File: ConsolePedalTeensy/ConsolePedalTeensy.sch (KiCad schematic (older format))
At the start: 27 parts, among them J1 Conn_02x25_Counter_Clockwise, SW1 SW_Push, SW2 SW_Push, U1 Teensy3.2, U2 LM7805_TO220

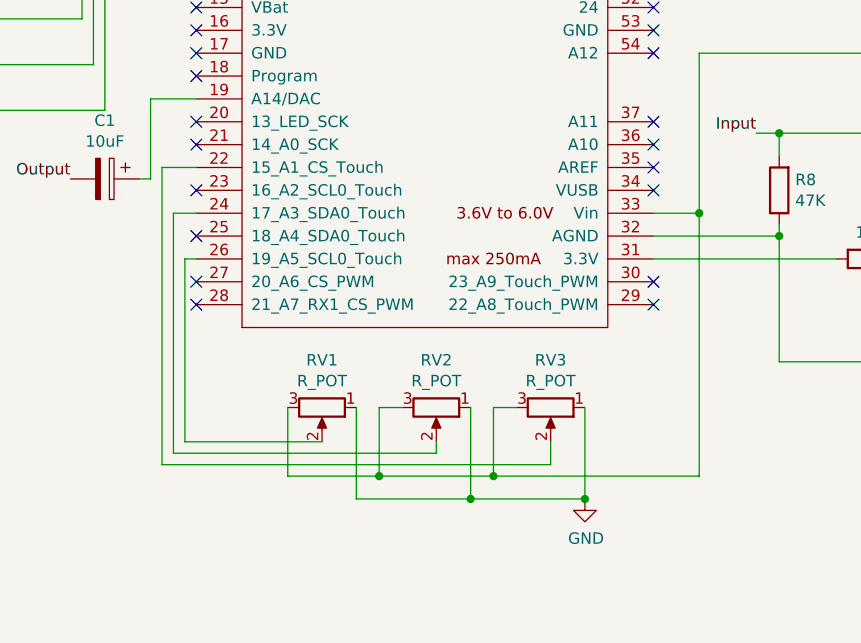
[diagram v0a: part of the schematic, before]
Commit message: Finished placement of components
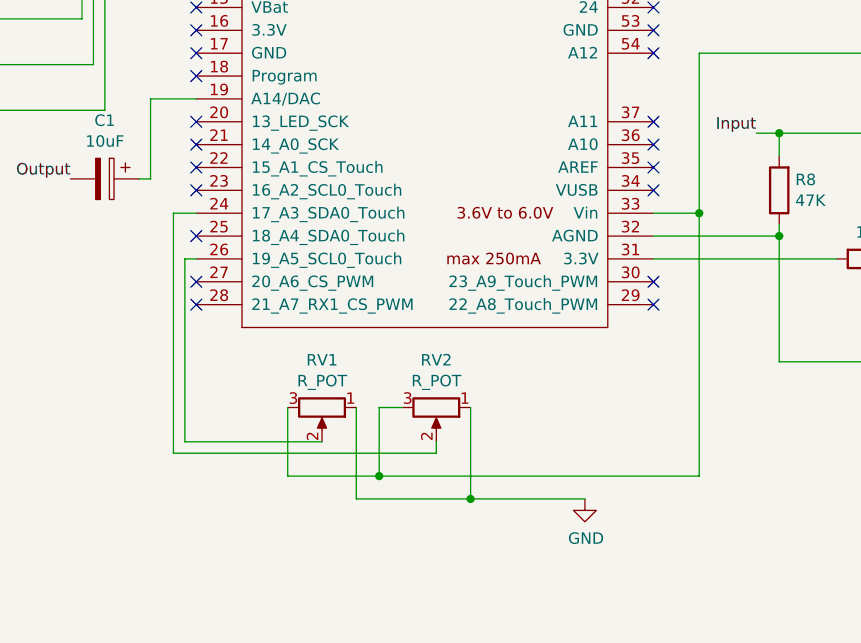
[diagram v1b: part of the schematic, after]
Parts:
- removed RV3: R_POT, Potentiometer_THT:Potentiometer_Bourns_PTV09A-1_Single_Vertical, symbol Device:R_POT
- U1: footprint teensy:Teensy30_31_32_All_Pins -> libraries:Teensy3.2
- U2: footprint Package_TO_SOT_THT:TO-220-3_Vertical -> Package_TO_SOT_THT:TO-220-3_Horizontal_TabDown
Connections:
- no-connect marks 64 -> 65
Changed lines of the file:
@@
 F 0 "U1" H 5200 4237 60  0000 C CNN
 F 1 "Teensy3.2" H 5200 4131 60  0000 C CNN
-F 2 "teensy:Teensy30_31_32_All_Pins" H 5200 1850 60  0001 C CNN
+F 2 "libraries:Teensy3.2" H 5200 1850 60  0001 C CNN
 F 3 "" H 5200 1850 60  0000 C CNN
 	1    5200 2600
@@
 F 0 "U2" H 7300 2142 50  0000 C CNN
 F 1 "LM7805_TO220" H 7300 2051 50  0000 C CNN
-F 2 "Package_TO_SOT_THT:TO-220-3_Vertical" H 7300 2125 50  0001 C CIN
+F 2 "Package_TO_SOT_THT:TO-220-3_Horizontal_TabDown" H 7300 2125 50  0001 C CIN
 F 3 "https://www.onsemi.cn/PowerSolutions/document/MC7800-D.PDF" H 7300 1850 50  0001 C CNN
 	1    7300 1900
@@
 	0    1    1    0
 $EndComp
-$Comp
-L Device:R_POT RV3
-U 1 1 602F1C1B
-P 5750 4400
-F 0 "RV3" V 5543 4400 50  0000 C CNN
-F 1 "R_POT" V 5634 4400 50  0000 C CNN
-F 2 "Potentiometer_THT:Potentiometer_Bourns_PTV09A-1_Single_Vertical" H 5750 4400 50  0001 C CNN
-F 3 "~" H 5750 4400 50  0001 C CNN
-	1    5750 4400
-	0    1    1    0
-$EndComp
 Wire Wire Line
 	4600 4400 4600 4700
@@
 Wire Wire Line
 	5000 4400 5100 4400
-Wire Wire Line
-	5600 4400 5500 4400
-Wire Wire Line
-	5500 4400 5500 4700
-Wire Wire Line
-	5500 4700 5000 4700
 Connection ~ 5000 4700
 Wire Wire Line
@@
 Wire Wire Line
 	5400 4800 5900 4800
-Wire Wire Line
-	5900 4800 5900 4400
 Connection ~ 5400 4800
 $Comp
@@
 	1    0    0    -1
 $EndComp
-Connection ~ 5900 4800
-Wire Wire Line
-	5500 4700 6400 4700
 Wire Wire Line
 	6400 4700 6400 3550
-Connection ~ 5500 4700
 Connection ~ 6400 3550
 Wire Wire Line
@@
 	5250 4600 4100 4600
 Wire Wire Line
-	5750 4550 5750 4650
-Wire Wire Line
-	5750 4650 4050 4650
-Wire Wire Line
 	4150 3750 4200 3750
 Wire Wire Line
@@
 Wire Wire Line
 	4100 3550 4100 4600
-Wire Wire Line
-	4050 3350 4200 3350
-Wire Wire Line
-	4050 3350 4050 4650
 $Comp
 L Device:LED_RGBC D3
@@
 NoConn ~ 6200 1350
 NoConn ~ 6200 1250
+Wire Wire Line
+	5000 4700 6400 4700
+NoConn ~ 4200 3350
 $EndSCHEMATC
